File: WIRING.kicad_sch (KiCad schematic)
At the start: 0 parts

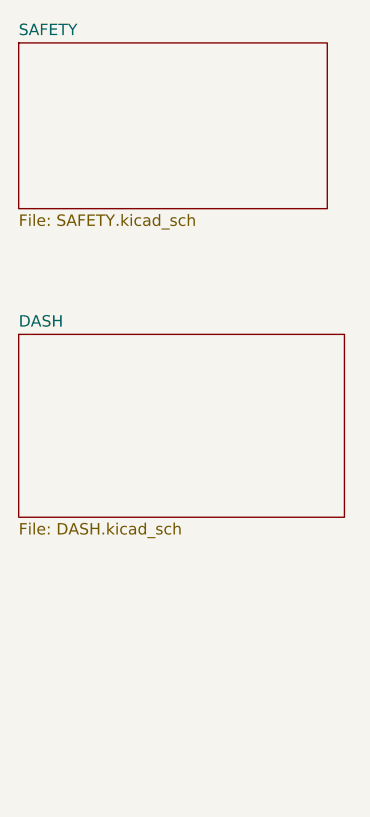
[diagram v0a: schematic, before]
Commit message: Relay layout done, pinout assignments, M1 Notes, and 04 Sch Start
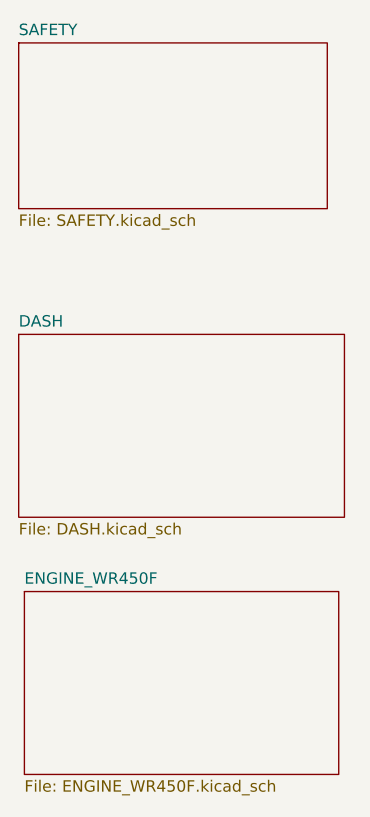
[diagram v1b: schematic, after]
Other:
- added sheet ENGINE_WR450F (ENGINE_WR450F.kicad_sch)
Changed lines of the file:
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@@
+		)
+	)
+	(sheet
+		(at 59.69 102.87)
+		(size 34.925 20.32)
+		(exclude_from_sim no)
+		(in_bom yes)
+		(on_board yes)
+		(dnp no)
+		(fields_autoplaced yes)
+		(stroke
+			(width 0.1524)
+			(type solid)
+		)
+		(fill
+			(color 0 0 0 0)
+		)
+		(property "Sheetname" "ENGINE_WR450F"
+			(at 59.69 102.1584 0)
+			(show_name no)
+			(do_not_autoplace no)
+			(effects
+				(font
+					(size 1.27 1.27)
+				)
+				(justify left bottom)
+			)
+		)
+		(property "Sheetfile" "ENGINE_WR450F.kicad_sch"
+			(at 59.69 123.7746 0)
+			(show_name no)
+			(do_not_autoplace no)
+			(effects
+				(font
+					(size 1.27 1.27)
+				)
+				(justify left top)
+			)
+		)
+		(instances
+			(project "Hub-2.0"
+				(path "/af8ad92e-80c5-47c7-b528-865d82af0364/399884b3-136d-40ca-bfde-e44c27866e82"
+					(page "9")
+				)
+			)
 		)
 	)
